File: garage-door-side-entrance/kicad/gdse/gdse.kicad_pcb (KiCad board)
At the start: 2 copper layers, 2 parts, among them J1 Screw_Terminal_01x10

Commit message: kicad work
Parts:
- A1: footprint Module:RaspberryPi_Pico_W_SMD_HandSolder -> Module:RaspberryPi_Pico_Common_THT
- moved J1 86.2 mm to (61.0, 76.2)
- moved A1 12.2 mm to (92.7, 71.1)
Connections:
- A1 pad 12: unconnected-(A1-GPIO9-Pad12) -> /Is Active LED | GP9 | 3-12
- A1 pad 14: unconnected-(A1-GPIO10-Pad14) -> /OD Cover Button | GP10 |4-14
- A1 pad 15: unconnected-(A1-GPIO11-Pad15) -> /Run LED | GP11 | 5-15
- A1 pad 16: unconnected-(A1-GPIO12-Pad16) -> /ID Cover Button | GP12 | 6-16
- A1 pad 17: unconnected-(A1-GPIO13-Pad17) -> /Locked LED | GP13 | 7-17
- A1 pad 19: unconnected-(A1-GPIO14-Pad19) -> /Locked Button | GP14 | 8-19
- A1 pad 36: Net-(A1-3V3) -> /3v3
- J1 pad 1: GND -> /3v3
- J1 pad 2: Net-(A1-3V3) -> GND
- J1 pad 3: unconnected-(J1-Is_Active_LED-Pad3) -> /Is Active LED | GP9 | 3-12
- J1 pad 4: unconnected-(J1-OD_Cover_Button-Pad4) -> /OD Cover Button | GP10 |4-14
- J1 pad 5: unconnected-(J1-Run_LED-Pad5) -> /Run LED | GP11 | 5-15
- J1 pad 6: unconnected-(J1-ID_Cover_Button-Pad6) -> /ID Cover Button | GP12 | 6-16
- J1 pad 7: unconnected-(J1-Unlocked_LED-Pad7) -> /Locked LED | GP13 | 7-17
- J1 pad 8: unconnected-(J1-Locked_LED-Pad8) -> /Locked Button | GP14 | 8-19
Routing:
- net /3v3: track 0.00 -> 91.8 mm, vias 0 -> 1
- net /Locked Button | GP14 | 8-19: track 0.00 -> 53.8 mm
- net /ID Cover Button | GP12 | 6-16: track 0.00 -> 52.1 mm
- net /Run LED | GP11 | 5-15: track 0.00 -> 51.3 mm
- net /OD Cover Button | GP10 |4-14: track 0.00 -> 51.3 mm
- net /Locked LED | GP13 | 7-17: track 0.00 -> 51.3 mm
- net /Is Active LED | GP9 | 3-12: track 0.00 -> 48.7 mm
- net GND: track 0.00 -> 34.3 mm
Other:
- board outline added: 101.3 x 150.7 mm

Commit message: kcad work
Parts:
- moved A1 2.84 mm to (94.0, 73.7)
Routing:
- net /Locked Button | GP14 | 8-19: track 53.8 -> 43.5 mm
- net /ID Cover Button | GP12 | 6-16: track 52.1 -> 42.5 mm
- net /Run LED | GP11 | 5-15: track 51.3 -> 42.5 mm
- net /Locked LED | GP13 | 7-17: track 51.3 -> 42.5 mm
- net /OD Cover Button | GP10 |4-14: track 51.3 -> 42.5 mm
- net /Is Active LED | GP9 | 3-12: track 48.7 -> 41.4 mm
- net /3v3: track 91.8 -> 88.2 mm
- net GND: track 34.3 -> 33.0 mm

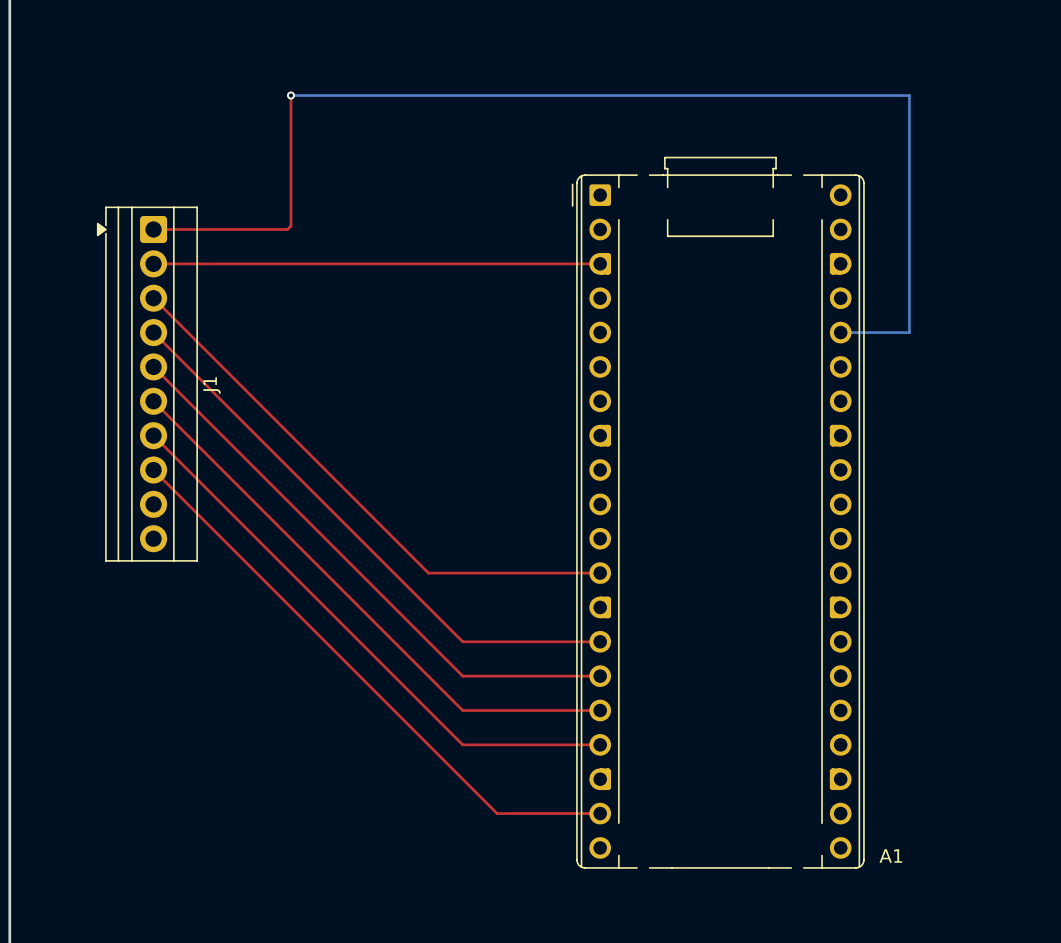
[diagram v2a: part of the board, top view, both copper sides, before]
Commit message: add jst xh connectors
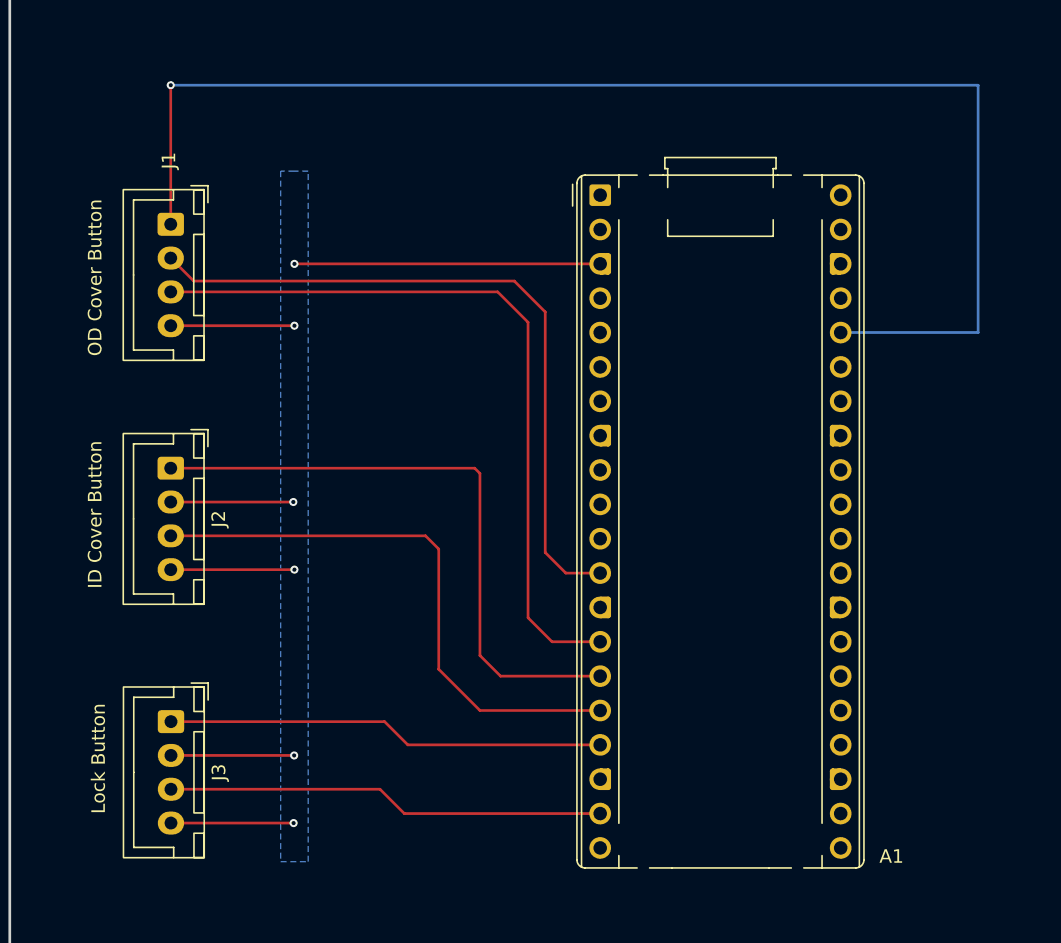
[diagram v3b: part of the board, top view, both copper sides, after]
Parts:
- added J2: Conn_01x04, Connector_JST:JST_XH_B4B-XH-A_1x04_P2.50mm_Vertical, F.Cu at (62.2, 93.8)
- added J3: Conn_01x04, Connector_JST:JST_XH_B4B-XH-A_1x04_P2.50mm_Vertical, F.Cu at (62.2, 112.6)
- J1: value Screw_Terminal_01x10 -> Conn_01x04; footprint TerminalBlock:TerminalBlock_Xinya_XY308-2.54-10P_1x10_P2.54mm_Horizontal -> Connector_JST:JST_XH_B4B-XH-A_1x04_P2.50mm_Vertical
- moved J1 1.33 mm to (62.2, 75.8)
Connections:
- J1 pad 2: GND -> /Is Active LED | GP9 | 3-12
- J1 pad 3: /Is Active LED | GP9 | 3-12 -> /OD Cover Button | GP10 |4-14
- J1 pad 4: /OD Cover Button | GP10 |4-14 -> GND
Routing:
- net GND: track 33.0 -> 68.4 mm, vias 0 -> 6
- net /OD Cover Button | GP10 |4-14: track 42.5 -> 55.3 mm
- net /Locked Button | GP14 | 8-19: track 43.5 -> 32.5 mm
- net /Is Active LED | GP9 | 3-12: track 41.4 -> 51.8 mm
- net /3v3: track 88.2 -> 98.4 mm
- net /Locked LED | GP13 | 7-17: track 42.5 -> 32.4 mm
- net /Run LED | GP11 | 5-15: track 42.5 -> 46.0 mm
- added copper zone on B.Cu, net GND
